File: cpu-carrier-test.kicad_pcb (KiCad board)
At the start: 2 copper layers, 64.3 x 103.3 mm, 91 parts, among them J1 Micro_SD_Card_Det, J1001 Conn_02x06_Odd_Even, J1101 USB_miniB, J1102 USB_C_Receptacle, J19 SFP, J20 SFP_CAGE, J4 JTAG, J5 Molex_0936263508, J6 USB_A, J99 Conn_02x06_Top_Bottom, SW1 SW_Push, U1 TXS0108EPW, U1101 USB3740B-AI9, U1102 UTC2000, U1103 FT232RL, U1104 74LVC1G00, U1105 SC185, U6 PCA9546AD, U8 74AC125, U9 TPS2051B

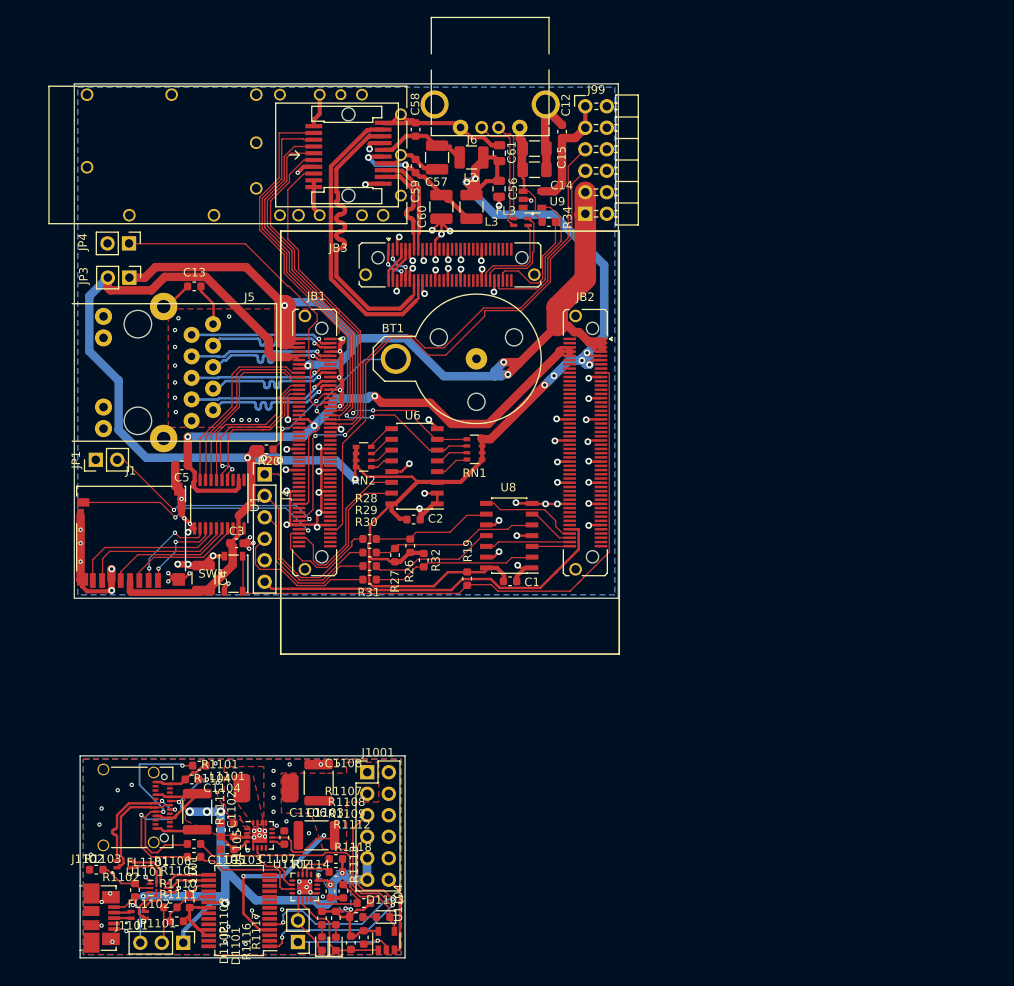
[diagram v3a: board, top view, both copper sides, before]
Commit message: final merge of power module; passes DRC
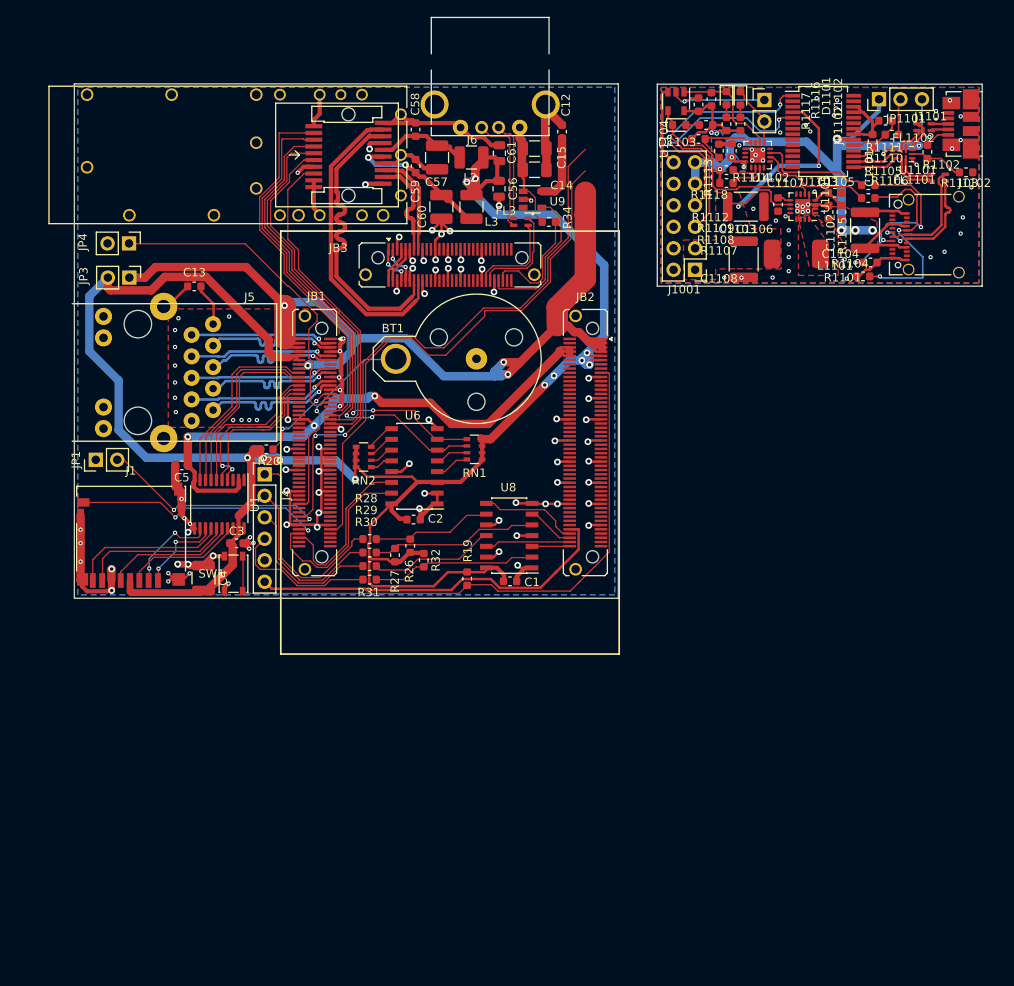
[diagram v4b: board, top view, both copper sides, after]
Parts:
- removed J99: Conn_02x06_Top_Bottom, pmod:PinHeader_2x06_P2.54mm_Horizontal
- moved J1101 138.3 mm to (217.4, 38.3), turned to 90 degrees
- moved R1103 131.8 mm to (218.0, 44.1), turned to 180 degrees
- moved FL1102 131.5 mm to (213.1, 38.7), turned to 180 degrees
- moved JP1101 129.3 mm to (207.7, 35.4), turned to 90 degrees
- moved R1102 128.0 mm to (213.4, 41.6), turned to 90 degrees
- moved R1111 126.4 mm to (208.5, 38.0), turned to 180 degrees
- moved FL1101 125.9 mm to (214.7, 44.7), turned to 180 degrees
- moved R1110 125.0 mm to (209.2, 39.6), turned to 180 degrees
- moved U1101 123.6 mm to (210.6, 41.9), turned to 90 degrees
- moved C1101 120.7 mm to (207.0, 40.4), turned to 90 degrees
- moved J1102 117.0 mm to (214.3, 51.4), turned to 90 degrees
- moved U1103 115.1 mm to (201.1, 39.2), turned to 0 degrees
- moved JP1102 113.8 mm to (194.2, 35.5), turned to 0 degrees
- moved R1105 112.5 mm to (206.4, 45.6), turned to 180 degrees
- moved D1102 111.5 mm to (191.3, 35.3), turned to 270 degrees
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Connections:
- C1101 pad 2: GND -> OTG_ID
- C1102 pad 2: GND -> OTG_ID
- C1103 pad 1: GND -> OTG_ID
- C1104 pad 2: GND -> OTG_ID
- C1105 pad 2: GND -> OTG_ID
- C1106 pad 1: VIN_3V3 -> +3V3_PWR_OUT
- C1106 pad 2: GND -> OTG_ID
- C1107 pad 2: GND -> OTG_ID
- C1108 pad 1: VIN_3V3 -> +3V3_PWR_OUT
- C1108 pad 2: GND -> OTG_ID
- J1001 pad 1: VIN_3V3 -> +3V3_PWR_OUT
- J1001 pad 10: GND -> OTG_ID
- J1001 pad 12: GND -> OTG_ID
- J1001 pad 2: GND -> OTG_ID
- J1001 pad 3: VIN_3V3 -> +3V3_PWR_OUT
- J1001 pad 4: GND -> OTG_ID
- J1001 pad 5: /power-and-uart/UART_TX_OUT -> UART_RX_MIO14
- J1001 pad 6: GND -> OTG_ID
- J1001 pad 7: /power-and-uart/UART_RX_IN -> UART_TX_MIO15
- J1001 pad 8: GND -> OTG_ID
- J1101 pad 5: GND -> OTG_ID
- J1101 pad 6: GND -> OTG_ID
- J1102 pad A1: GND -> OTG_ID
- J1102 pad A12: GND -> OTG_ID
- J1102 pad B1: GND -> OTG_ID
- J1102 pad B12: GND -> OTG_ID
- J1102 pad S1: GND -> OTG_ID
- JB1 pad 14: VIN -> +3V3_PWR_OUT
- JB1 pad 16: VIN -> +3V3_PWR_OUT
- JB1 pad 2: VIN -> +3V3_PWR_OUT
- JB1 pad 4: VIN -> +3V3_PWR_OUT
- JB1 pad 6: VIN -> +3V3_PWR_OUT
- JB2 pad 1: VIN -> +3V3_PWR_OUT
- JB2 pad 3: VIN -> +3V3_PWR_OUT
- JB2 pad 5: VIN -> +3V3_PWR_OUT
- JB2 pad 7: VIN -> +3V3_PWR_OUT
- JP3 pad 1: VIN -> +3V3_PWR_OUT
- L1101 pad 1: VIN_3V3 -> +3V3_PWR_OUT
- R1101 pad 2: GND -> OTG_ID
- R1103 pad 1: GND -> OTG_ID
- R1104 pad 2: GND -> OTG_ID
- R1109 pad 2: GND -> OTG_ID
- R1111 pad 2: GND -> OTG_ID
- U1101 pad 3: GND -> OTG_ID
- U1101 pad 8: GND -> OTG_ID
- U1102 pad 13: GND -> OTG_ID
- U1102 pad 17: GND -> OTG_ID
- U1103 pad 1: /power-and-uart/UART_TX_OUT -> UART_RX_MIO14
- U1103 pad 18: GND -> OTG_ID
- U1103 pad 21: GND -> OTG_ID
- U1103 pad 25: GND -> OTG_ID
- U1103 pad 26: GND -> OTG_ID
- U1103 pad 4: VIN_3V3 -> +3V3_PWR_OUT
- U1103 pad 5: /power-and-uart/UART_RX_IN -> UART_TX_MIO15
- U1103 pad 7: GND -> OTG_ID
- U1104 pad 3: GND -> OTG_ID
- U1105 pad 10: VIN_3V3 -> +3V3_PWR_OUT
- U1105 pad 11: GND -> OTG_ID
- U1105 pad 12: GND -> OTG_ID
- U1105 pad 13: GND -> OTG_ID
- U1105 pad 17: GND -> OTG_ID
- U1105 pad 3: GND -> OTG_ID
- U1105 pad 5: GND -> OTG_ID
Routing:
- net +3V3_PWR_OUT: track 0.00 -> 141.0 mm, vias 0 -> 6
- net VIN: track 111.6 -> 0.00 mm, vias 4 -> 0
- net Net-(C14-Pad1): track 102.9 -> 12.4 mm, vias 10 -> 0
- net +5V: track 13.9 -> 98.7 mm, vias 0 -> 10
- net Net-(FL3-Pad3): track 59.8 -> 14.6 mm, vias 43 -> 0
- net OTG_ID: track 226.8 -> 267.4 mm, vias 93 -> 136
- net PHY_MDIO0_N: track 48.9 -> 17.0 mm, vias 3 -> 1
- net UART_RX_MIO14: track 64.6 -> 96.4 mm, vias 0 -> 2
- net PHY_MDIO1_N: track 46.4 -> 17.0 mm, vias 3 -> 1
- net PHY_MDIO1_P: track 45.7 -> 17.1 mm, vias 3 -> 1
- net Net-(J1102-PadB5): track 0.00 -> 24.7 mm, vias 0 -> 2
- net SCL1: track 79.2 -> 54.5 mm, vias 4 -> 2
- net SD0_D2_MIO44: track 46.8 -> 22.8 mm
- net Net-(D1103-Pad1): track 0.00 -> 24.0 mm
- net Net-(J1102-PadA5): track 0.00 -> 23.2 mm, vias 0 -> 3
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- added copper zone on F.Cu, net +3V3_PWR_OUT
- removed copper zone on B.Cu, net GND
- removed copper zone on F.Cu, net GND
- removed copper zone on F.Cu, net VIN_3V3
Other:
- board size 64.3 x 103.3 mm -> 107.3 x 60.8 mm

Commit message: integrated power/uart sub-board and fixed design rule violatons
(new violations due to jlcpcb's 0.5mm hole distance)
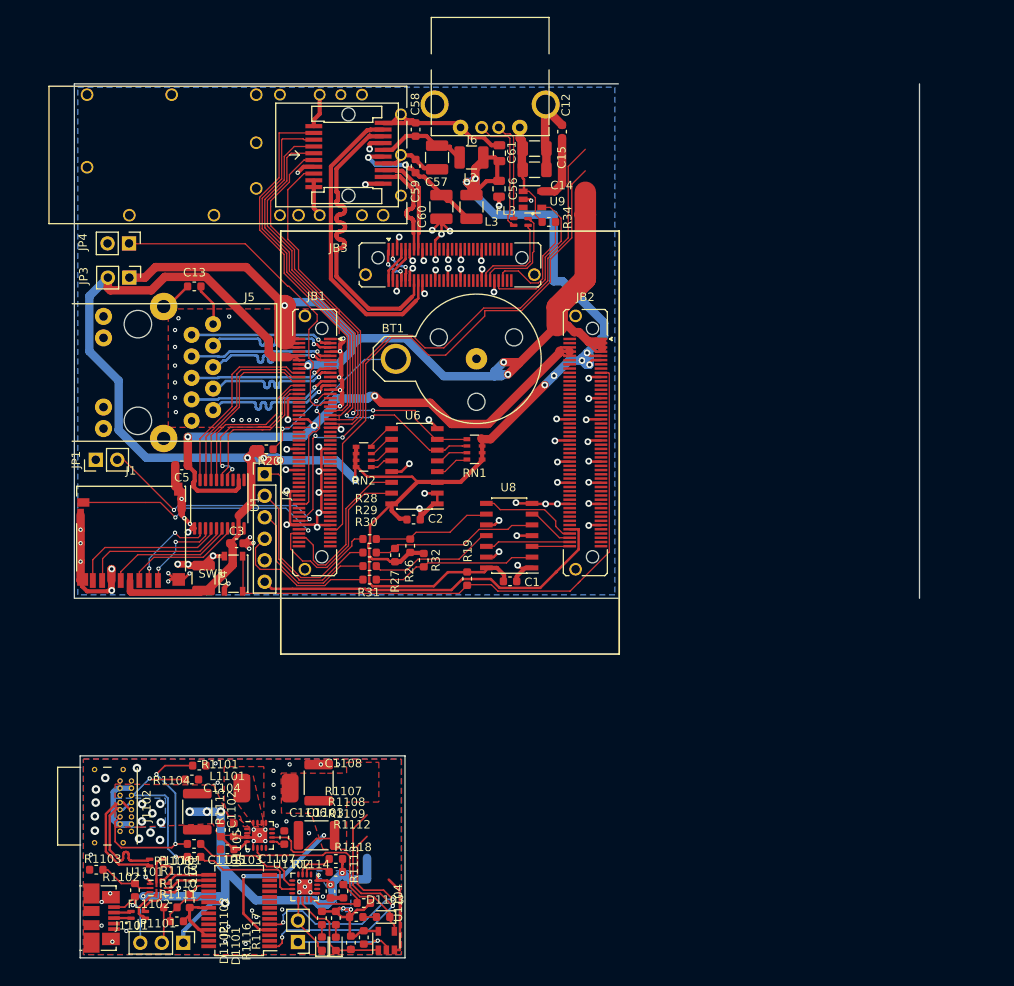
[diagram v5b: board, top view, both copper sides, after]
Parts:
- removed J1001: Conn_02x06_Odd_Even, Connector_PinHeader_2.54mm:PinHeader_2x06_P2.54mm_Vertical
- J1102: value USB_C_Receptacle -> USB_C_Receptacle_USB2.0; footprint Connector_USB:USB_C_Receptacle_Amphenol_12401610E4-2A_CircularHoles -> proj_footprints:USB_C_Receptacle_GCT_USB4085_smaller_holes
- moved J1101 138.3 mm to (115.8, 132.2), turned to 270 degrees
- moved R1103 131.8 mm to (115.2, 126.5), turned to 0 degrees
- moved FL1102 131.5 mm to (120.1, 131.8), turned to 0 degrees
- moved JP1101 129.3 mm to (125.5, 135.1), turned to 270 degrees
- moved R1102 128.0 mm to (119.8, 128.9), turned to 270 degrees
- moved R1111 126.4 mm to (124.7, 132.6), turned to 0 degrees
- moved R1110 125.0 mm to (124.0, 130.9), turned to 0 degrees
- moved U1101 123.6 mm to (122.6, 128.7), turned to 270 degrees
- moved FL1101 122.8 mm to (122.3, 125.7), turned to 0 degrees
- moved C1101 120.7 mm to (126.2, 130.2), turned to 270 degrees
- moved U1103 115.1 mm to (132.1, 131.3), turned to 180 degrees
- moved J1102 114.8 mm to (119.3, 116.0), turned to 270 degrees
- moved JP1102 113.8 mm to (139.0, 135.0), turned to 180 degrees
- moved R1105 112.5 mm to (126.7, 125.0), turned to 0 degrees
- moved D1102 111.5 mm to (141.9, 135.2), turned to 90 degrees
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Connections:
- FL1101 pad 1: /power-and-uart/Sheet5C4CE702/USB_C_D_P -> /power-and-uart/Sheet5C4CE702/USB_C_D_N
- FL1101 pad 2: /power-and-uart/Sheet5C4CE702/USB1_P -> /power-and-uart/Sheet5C4CE702/USB1_N
- FL1101 pad 3: /power-and-uart/Sheet5C4CE702/USB1_N -> /power-and-uart/Sheet5C4CE702/USB1_P
- FL1101 pad 4: /power-and-uart/Sheet5C4CE702/USB_C_D_N -> /power-and-uart/Sheet5C4CE702/USB_C_D_P
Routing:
- net OTG_ID: track 267.4 -> 255.6 mm, vias 136 -> 140
- net Net-(J1102-PadA5): track 23.2 -> 20.2 mm, vias 3 -> 2
- net /power-and-uart/Sheet5C4CE702/USB1_N: track 5.41 -> 3.47 mm
- net +5V: track 98.7 -> 96.8 mm, vias 10 -> 15
- net Net-(J1102-PadB5): track 24.7 -> 26.0 mm
- net /power-and-uart/Sheet5C4CE702/USB_C_D_P: track 13.0 -> 14.3 mm
- net /power-and-uart/Sheet5C4CE702/USB1_P: track 4.65 -> 3.39 mm
- net +3V3: track 255.3 -> 255.9 mm
- net PHY_MDIO0_P: track 16.9 -> 17.4 mm
- net /power-and-uart/Sheet5C4CE702/USB_C_D_N: track 14.6 -> 14.3 mm, vias 2 -> 0
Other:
- board size 107.3 x 60.8 mm -> 99.9 x 103.3 mm
- net class Default: clearance 0.153 -> 0.1524
- net class diffp added: clearance 0.1778, trace_width 0.2794, via_dia 0.508, via_drill 0.254
- rule trace_clearance: 0.153 -> 0.1524

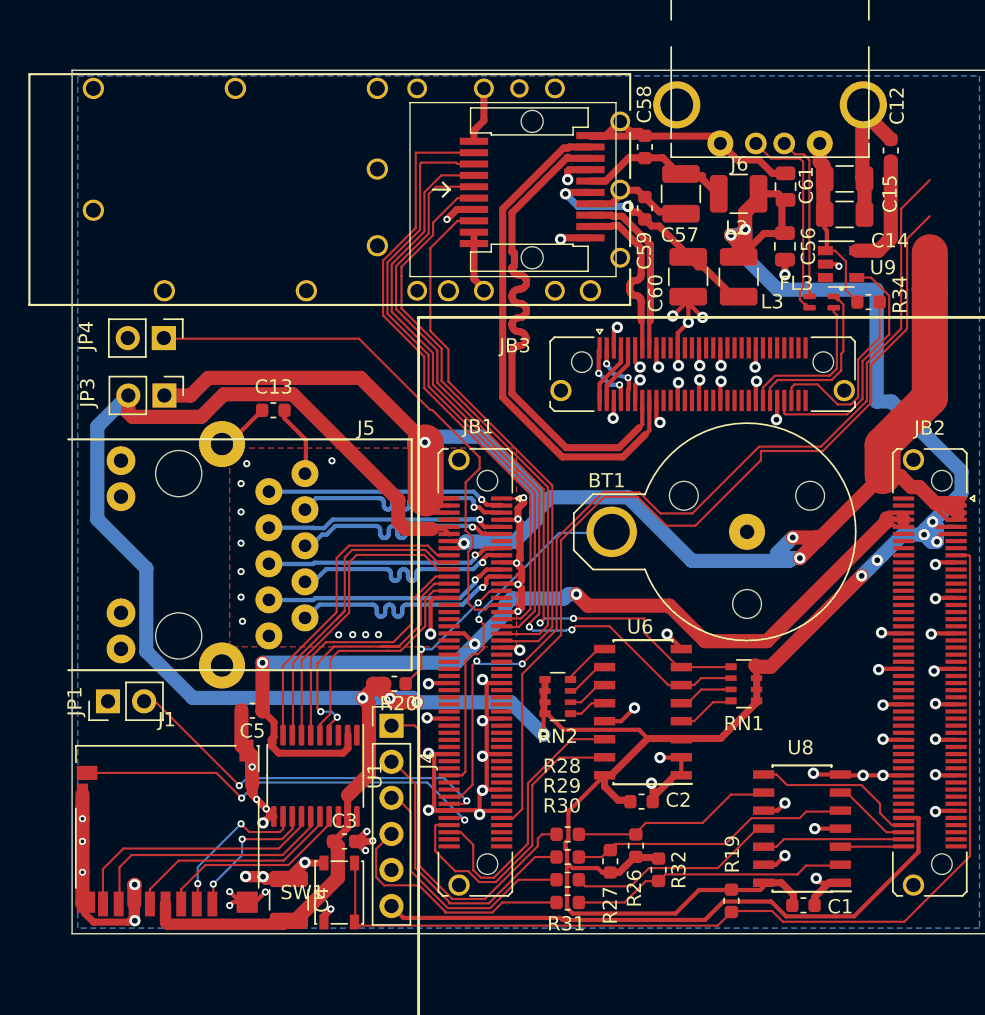
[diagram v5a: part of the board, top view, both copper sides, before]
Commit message: rotated SDIO to face board front
this allows the power module to be either positioned at its
original location or -- alternatively, next to the SDIO card
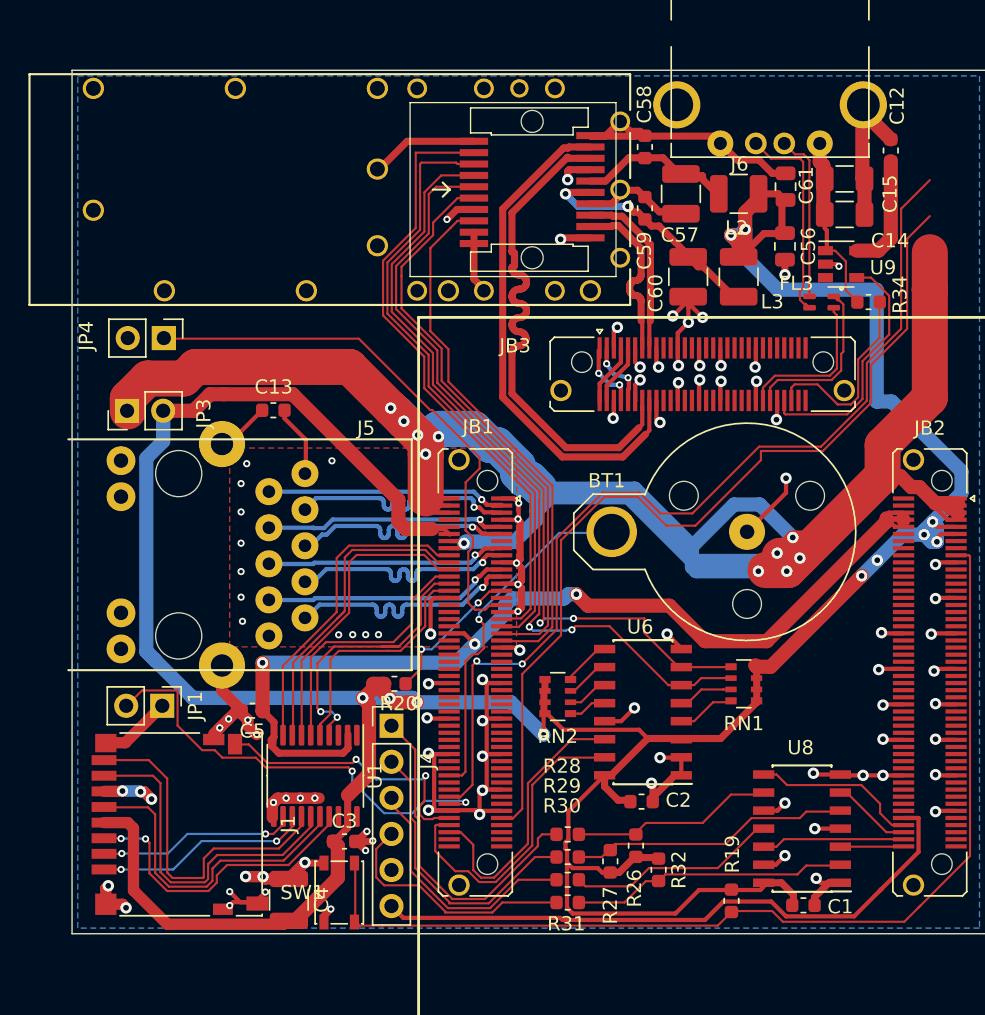
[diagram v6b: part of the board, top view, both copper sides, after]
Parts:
- J1: footprint Connector_Card:microSD_HC_Hirose_DM3D-SF -> proj_footprints:microSD_HC_Hirose_DM3D-SF_smaller_crtyd
- moved JP1 3.83 mm to (119.0, 78.3), turned to 270 degrees
- moved JP3 2.84 mm to (116.5, 57.6), turned to 90 degrees
- moved J1 0.93 mm to (120.2, 86.7), turned to 270 degrees
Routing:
- net +3V3_PWR_OUT: track 141.0 -> 205.6 mm, vias 6 -> 13
- net MIO_9: track 30.0 -> 19.9 mm
- net OTG_ID: track 255.6 -> 263.5 mm, vias 140 -> 145
- net Net-(J1-Pad3): track 14.0 -> 21.5 mm, vias 0 -> 2
- net Net-(J1-Pad5): track 15.7 -> 23.1 mm
- net Net-(J1-Pad7): track 17.9 -> 24.4 mm
- net Net-(J1-Pad8): track 18.4 -> 24.3 mm
- net Net-(J1-Pad1): track 9.93 -> 15.2 mm
- net MIO_0: track 26.6 -> 31.4 mm
- net Net-(J1-Pad2): track 10.9 -> 14.0 mm
- net +3V3: track 255.9 -> 258.5 mm
- net Net-(J4-Pad1): track 24.4 -> 23.5 mm
